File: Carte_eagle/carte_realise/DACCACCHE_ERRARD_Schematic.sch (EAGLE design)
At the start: 10 parts, among them CON1 CON-1X2-SPOX-M-2.50, CON2 CON-1X2-SPOX-M-2.50, U1 DOGM163

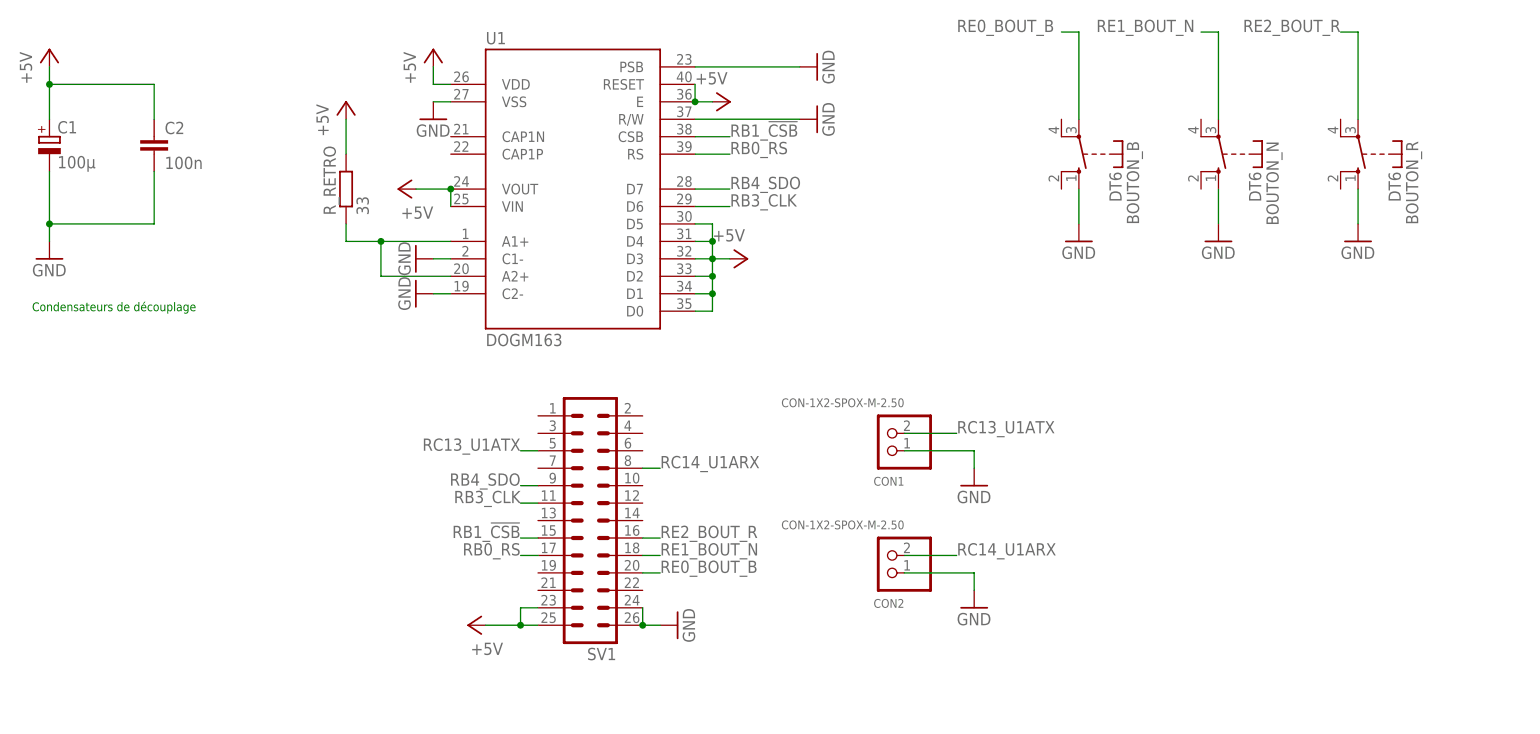
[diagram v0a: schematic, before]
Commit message: Modification de schematics eagle
Rajout des commentaires sur le schéma
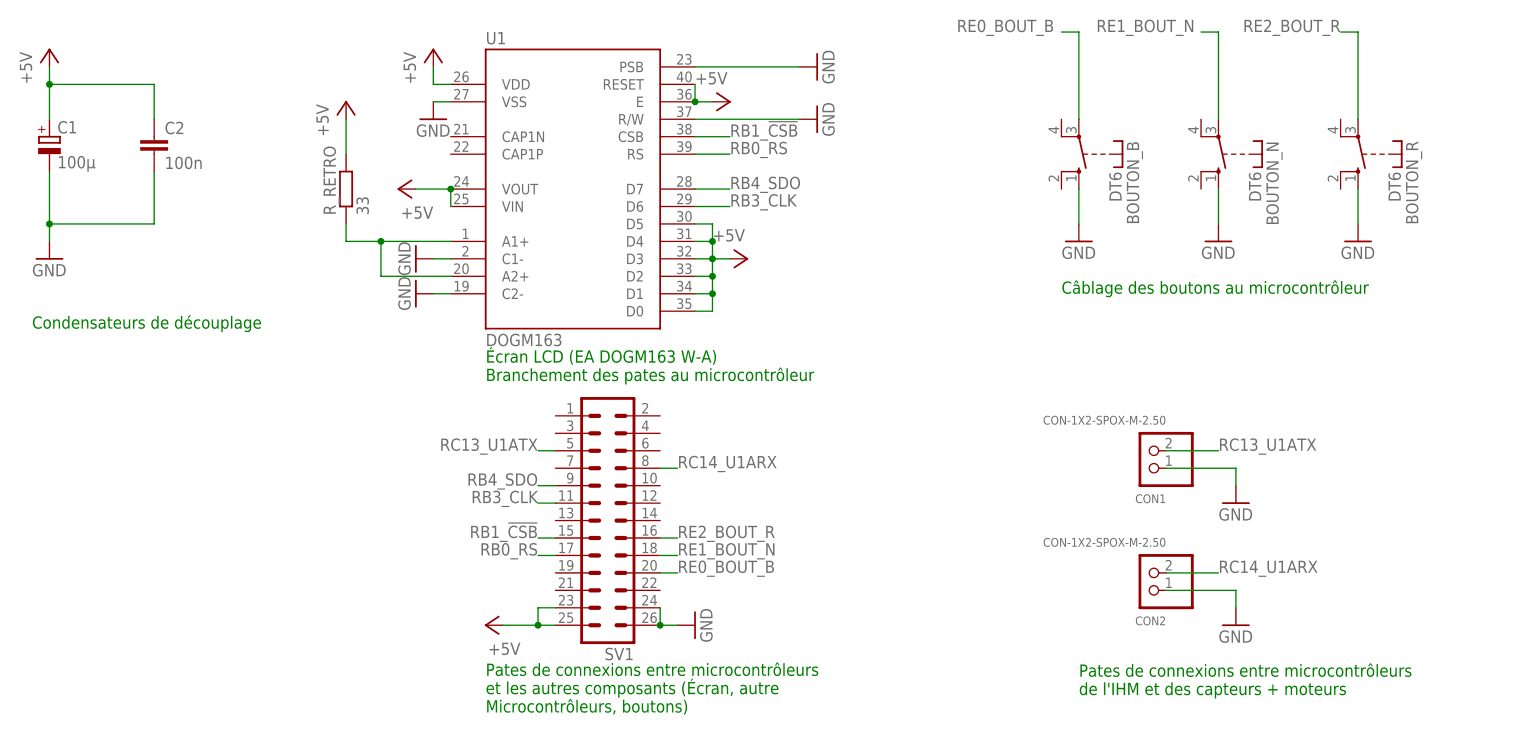
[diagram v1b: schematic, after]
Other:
- note added: "Câblage des boutons au microcontrôleur"
- note added: "Pates de connexions entre microcontrôleurs de l'IHM et des capteurs + moteurs"
- note added: "Pates de connexions entre microcontrôleurs et les autres composants (Écran, autre Microcontrôleurs, boutons)"
- note added: "Écran LCD (EA DOGM163 W-A) Branchement des pates au microcontrôleur"
- moved on the sheet: CON1, CON2, SV1
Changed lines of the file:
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@@
 <sheet>
 <plain>
-<text x="-20.32" y="38.1" size="1.27" layer="91">Condensateurs de découplage</text>
+<text x="45.72" y="27.94" size="1.778" layer="91">Écran LCD (EA DOGM163 W-A)
+Branchement des pates au microcontrôleur</text>
+<text x="129.54" y="40.64" size="1.778" layer="91">Câblage des boutons au microcontrôleur</text>
+<text x="132.08" y="-17.78" size="1.778" layer="91">Pates de connexions entre microcontrôleurs
+de l'IHM et des capteurs + moteurs</text>
+<text x="45.72" y="-20.32" size="1.778" layer="91">Pates de connexions entre microcontrôleurs
+et les autres composants (Écran, autre
+Microcontrôleurs, boutons)</text>
+<text x="-20.32" y="35.56" size="1.778" layer="91">Condensateurs de découplage</text>
 </plain>
 <instances>
 <instance part="U1" gate="G$1" x="58.42" y="55.88"/>
-<instance part="SV1" gate="1" x="60.96" y="7.62" rot="R180"/>
+<instance part="SV1" gate="1" x="63.5" y="7.62" rot="R180"/>
 <instance part="GND2" gate="1" x="93.98" y="73.66" rot="R90"/>
-<instance part="GND3" gate="1" x="73.66" y="-7.62" rot="R90"/>
+<instance part="GND3" gate="1" x="76.2" y="-7.62" rot="R90"/>
 <instance part="P+1" gate="1" x="33.02" y="55.88" rot="R90"/>
 <instance part="P+2" gate="1" x="81.28" y="68.58" rot="R270"/>
@@
 <instance part="GND7" gate="1" x="152.4" y="48.26"/>
 <instance part="GND8" gate="1" x="132.08" y="48.26"/>
-<instance part="GND10" gate="1" x="116.84" y="12.7"/>
-<instance part="CON1" gate="G$1" x="104.14" y="20.32" rot="R180"/>
-<instance part="CON2" gate="G$1" x="104.14" y="2.54" rot="R180"/>
-<instance part="P+9" gate="1" x="43.18" y="-7.62" rot="R90"/>
+<instance part="GND10" gate="1" x="154.94" y="10.16"/>
+<instance part="CON1" gate="G$1" x="142.24" y="17.78" rot="R180"/>
+<instance part="CON2" gate="G$1" x="142.24" y="0" rot="R180"/>
+<instance part="P+9" gate="1" x="45.72" y="-7.62" rot="R90"/>
 <instance part="C2" gate="G$1" x="-2.54" y="63.5"/>
-<instance part="GND9" gate="1" x="116.84" y="-5.08"/>
+<instance part="GND9" gate="1" x="154.94" y="-7.62"/>
 <instance part="GND11" gate="1" x="35.56" y="40.64" rot="R270"/>
 <instance part="GND12" gate="1" x="35.56" y="45.72" rot="R270"/>
@@
 <pinref part="P+9" gate="1" pin="+5V"/>
 <pinref part="SV1" gate="1" pin="25"/>
-<wire x1="45.72" y1="-7.62" x2="50.8" y2="-7.62" width="0.1524" layer="91"/>
+<wire x1="48.26" y1="-7.62" x2="53.34" y2="-7.62" width="0.1524" layer="91"/>
 <pinref part="SV1" gate="1" pin="23"/>
-<wire x1="50.8" y1="-7.62" x2="53.34" y2="-7.62" width="0.1524" layer="91"/>
-<wire x1="53.34" y1="-5.08" x2="50.8" y2="-5.08" width="0.1524" layer="91"/>
-<wire x1="50.8" y1="-5.08" x2="50.8" y2="-7.62" width="0.1524" layer="91"/>
-<junction x="50.8" y="-7.62"/>
+<wire x1="53.34" y1="-7.62" x2="55.88" y2="-7.62" width="0.1524" layer="91"/>
+<wire x1="55.88" y1="-5.08" x2="53.34" y2="-5.08" width="0.1524" layer="91"/>
+<wire x1="53.34" y1="-5.08" x2="53.34" y2="-7.62" width="0.1524" layer="91"/>
+<junction x="53.34" y="-7.62"/>
 </segment>
 <segment>
@@
 <pinref part="SV1" gate="1" pin="24"/>
 <pinref part="SV1" gate="1" pin="26"/>
-<wire x1="68.58" y1="-5.08" x2="68.58" y2="-7.62" width="0.1524" layer="91"/>
+<wire x1="71.12" y1="-5.08" x2="71.12" y2="-7.62" width="0.1524" layer="91"/>
 <pinref part="GND3" gate="1" pin="GND"/>
-<wire x1="71.12" y1="-7.62" x2="68.58" y2="-7.62" width="0.1524" layer="91"/>
-<junction x="68.58" y="-7.62"/>
+<wire x1="73.66" y1="-7.62" x2="71.12" y2="-7.62" width="0.1524" layer="91"/>
+<junction x="71.12" y="-7.62"/>
 </segment>
 <segment>
@@
 <segment>
 <pinref part="GND9" gate="1" pin="GND"/>
-<wire x1="116.84" y1="0" x2="116.84" y2="-2.54" width="0.1524" layer="91"/>
+<wire x1="154.94" y1="-2.54" x2="154.94" y2="-5.08" width="0.1524" layer="91"/>
 <pinref part="CON2" gate="G$1" pin="1"/>
-<wire x1="106.68" y1="0" x2="116.84" y2="0" width="0.1524" layer="91"/>
+<wire x1="144.78" y1="-2.54" x2="154.94" y2="-2.54" width="0.1524" layer="91"/>
 </segment>
 <segment>
 <pinref part="GND10" gate="1" pin="GND"/>
 <pinref part="CON1" gate="G$1" pin="1"/>
-<wire x1="106.68" y1="17.78" x2="116.84" y2="17.78" width="0.1524" layer="91"/>
-<wire x1="116.84" y1="17.78" x2="116.84" y2="15.24" width="0.1524" layer="91"/>
+<wire x1="144.78" y1="15.24" x2="154.94" y2="15.24" width="0.1524" layer="91"/>
+<wire x1="154.94" y1="15.24" x2="154.94" y2="12.7" width="0.1524" layer="91"/>
 </segment>
 <segment>
@@
 <segment>
 <pinref part="SV1" gate="1" pin="9"/>
-<wire x1="53.34" y1="12.7" x2="50.8" y2="12.7" width="0.1524" layer="91"/>
-<label x="50.8" y="12.7" size="1.778" layer="95" rot="MR0"/>
+<wire x1="55.88" y1="12.7" x2="53.34" y2="12.7" width="0.1524" layer="91"/>
+<label x="53.34" y="12.7" size="1.778" layer="95" rot="MR0"/>
 </segment>
 <segment>
@@
 <segment>
 <pinref part="SV1" gate="1" pin="11"/>
-<wire x1="53.34" y1="10.16" x2="50.8" y2="10.16" width="0.1524" layer="91"/>
-<label x="50.8" y="10.16" size="1.778" layer="95" rot="MR0"/>
+<wire x1="55.88" y1="10.16" x2="53.34" y2="10.16" width="0.1524" layer="91"/>
+<label x="53.34" y="10.16" size="1.778" layer="95" rot="MR0"/>
 </segment>
 <segment>
@@
 <segment>
 <pinref part="SV1" gate="1" pin="15"/>
-<wire x1="53.34" y1="5.08" x2="50.8" y2="5.08" width="0.1524" layer="91"/>
-<label x="50.8" y="5.08" size="1.778" layer="95" rot="MR0"/>
+<wire x1="55.88" y1="5.08" x2="53.34" y2="5.08" width="0.1524" layer="91"/>
+<label x="53.34" y="5.08" size="1.778" layer="95" rot="MR0"/>
 </segment>
 <segment>
@@
 <segment>
 <pinref part="SV1" gate="1" pin="17"/>
-<wire x1="53.34" y1="2.54" x2="50.8" y2="2.54" width="0.1524" layer="91"/>
-<label x="50.8" y="2.54" size="1.778" layer="95" rot="MR0"/>
+<wire x1="55.88" y1="2.54" x2="53.34" y2="2.54" width="0.1524" layer="91"/>
+<label x="53.34" y="2.54" size="1.778" layer="95" rot="MR0"/>
 </segment>
 <segment>
@@
 <segment>
 <pinref part="SV1" gate="1" pin="16"/>
-<wire x1="68.58" y1="5.08" x2="71.12" y2="5.08" width="0.1524" layer="91"/>
-<label x="71.12" y="5.08" size="1.778" layer="95"/>
+<wire x1="71.12" y1="5.08" x2="73.66" y2="5.08" width="0.1524" layer="91"/>
+<label x="73.66" y="5.08" size="1.778" layer="95"/>
 </segment>
 <segment>
@@
 <segment>
 <pinref part="SV1" gate="1" pin="18"/>
-<wire x1="68.58" y1="2.54" x2="71.12" y2="2.54" width="0.1524" layer="91"/>
-<label x="71.12" y="2.54" size="1.778" layer="95"/>
+<wire x1="71.12" y1="2.54" x2="73.66" y2="2.54" width="0.1524" layer="91"/>
+<label x="73.66" y="2.54" size="1.778" layer="95"/>
 </segment>
 <segment>
@@
 <segment>
 <pinref part="SV1" gate="1" pin="20"/>
-<wire x1="68.58" y1="0" x2="71.12" y2="0" width="0.1524" layer="91"/>
-<label x="71.12" y="0" size="1.778" layer="95"/>
+<wire x1="71.12" y1="0" x2="73.66" y2="0" width="0.1524" layer="91"/>
+<label x="73.66" y="0" size="1.778" layer="95"/>
 </segment>
 <segment>
@@
 <segment>
 <pinref part="SV1" gate="1" pin="5"/>
-<wire x1="53.34" y1="17.78" x2="50.8" y2="17.78" width="0.1524" layer="91"/>
-<label x="50.8" y="17.78" size="1.778" layer="95" rot="MR0"/>
+<wire x1="55.88" y1="17.78" x2="53.34" y2="17.78" width="0.1524" layer="91"/>
+<label x="53.34" y="17.78" size="1.778" layer="95" rot="MR0"/>
 </segment>
 <segment>
 <pinref part="CON1" gate="G$1" pin="2"/>
-<wire x1="106.68" y1="20.32" x2="114.3" y2="20.32" width="0.1524" layer="91"/>
-<label x="114.3" y="20.32" size="1.778" layer="95"/>
+<wire x1="144.78" y1="17.78" x2="152.4" y2="17.78" width="0.1524" layer="91"/>
+<label x="152.4" y="17.78" size="1.778" layer="95"/>
 </segment>
 </net>
@@
 <segment>
 <pinref part="SV1" gate="1" pin="8"/>
-<wire x1="68.58" y1="15.24" x2="71.12" y2="15.24" width="0.1524" layer="91"/>
-<label x="71.12" y="15.24" size="1.778" layer="95"/>
+<wire x1="71.12" y1="15.24" x2="73.66" y2="15.24" width="0.1524" layer="91"/>
+<label x="73.66" y="15.24" size="1.778" layer="95"/>
 </segment>
 <segment>
 <pinref part="CON2" gate="G$1" pin="2"/>
-<wire x1="106.68" y1="2.54" x2="114.3" y2="2.54" width="0.1524" layer="91"/>
-<label x="114.3" y="2.54" size="1.778" layer="95"/>
+<wire x1="144.78" y1="0" x2="152.4" y2="0" width="0.1524" layer="91"/>
+<label x="152.4" y="0" size="1.778" layer="95"/>
 </segment>
 </net>
@@
 </schematic>
 </drawing>
+<compatibility>
+<note version="6.3" minversion="6.2.2" severity="warning">
+Since Version 6.2.2 text objects can contain more than one line,
+which will not be processed correctly with this version.
+</note>
+</compatibility>
 </eagle>

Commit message: update board et schematics
finalisation du schema avec le changement des pins de l'ecran et des boutons
finalisation de la carte avec l'epaisseur des cables et le cassage des angles droits
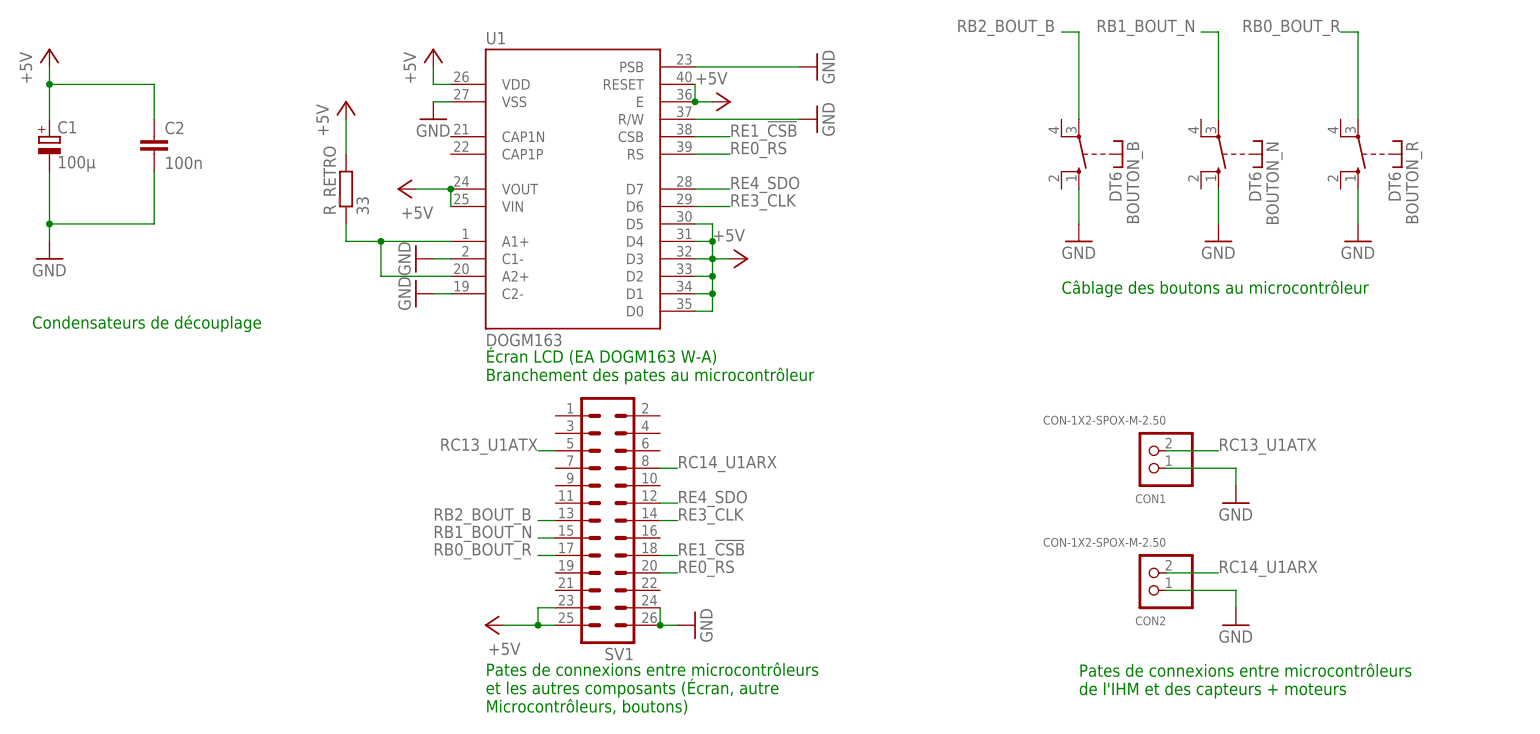
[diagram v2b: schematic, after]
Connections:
- net N$1 renamed RHETRO_RES
- removed net RB0_RS: SV1.17, U1.RS
- removed net RB1_!CSB: SV1.15, U1.CSB
- removed net RB3_CLK: SV1.11, U1.D6
- removed net RB4_SDO: SV1.9, U1.D7
- removed net RE0_BOUT_B: BOUTON_B.P, SV1.20
- removed net RE1_BOUT_N: BOUTON_N.P, SV1.18
- removed net RE2_BOUT_R: BOUTON_R.P, SV1.16
- new net RB0_BOUT_R: BOUTON_R.P, SV1.17
- new net RB1_BOUT_N: BOUTON_N.P, SV1.15
- new net RB2_BOUT_B: BOUTON_B.P, SV1.13
- new net RE0_RS: SV1.20, U1.RS
- new net RE1_!CSB: SV1.18, U1.CSB
- new net RE3_CLK: SV1.14, U1.D6
- new net RE4_SDO: SV1.12, U1.D7
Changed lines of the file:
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@@
 </segment>
 </net>
-<net name="RB4_SDO" class="0">
-<segment>
-<pinref part="SV1" gate="1" pin="9"/>
-<wire x1="55.88" y1="12.7" x2="53.34" y2="12.7" width="0.1524" layer="91"/>
-<label x="53.34" y="12.7" size="1.778" layer="95" rot="MR0"/>
-</segment>
-<segment>
-<pinref part="U1" gate="G$1" pin="D7"/>
-<wire x1="76.2" y1="55.88" x2="81.28" y2="55.88" width="0.1524" layer="91"/>
-<label x="81.28" y="55.88" size="1.778" layer="95"/>
-</segment>
-</net>
-<net name="RB3_CLK" class="0">
-<segment>
-<pinref part="SV1" gate="1" pin="11"/>
-<wire x1="55.88" y1="10.16" x2="53.34" y2="10.16" width="0.1524" layer="91"/>
-<label x="53.34" y="10.16" size="1.778" layer="95" rot="MR0"/>
-</segment>
-<segment>
-<pinref part="U1" gate="G$1" pin="D6"/>
-<wire x1="76.2" y1="53.34" x2="81.28" y2="53.34" width="0.1524" layer="91"/>
-<label x="81.28" y="53.34" size="1.778" layer="95"/>
-</segment>
-</net>
-<net name="RB1_!CSB" class="0">
-<segment>
-<pinref part="SV1" gate="1" pin="15"/>
-<wire x1="55.88" y1="5.08" x2="53.34" y2="5.08" width="0.1524" layer="91"/>
-<label x="53.34" y="5.08" size="1.778" layer="95" rot="MR0"/>
-</segment>
-<segment>
-<pinref part="U1" gate="G$1" pin="CSB"/>
-<wire x1="76.2" y1="63.5" x2="81.28" y2="63.5" width="0.1524" layer="91"/>
-<label x="81.28" y="63.5" size="1.778" layer="95"/>
-</segment>
-</net>
-<net name="RB0_RS" class="0">
-<segment>
-<pinref part="SV1" gate="1" pin="17"/>
-<wire x1="55.88" y1="2.54" x2="53.34" y2="2.54" width="0.1524" layer="91"/>
-<label x="53.34" y="2.54" size="1.778" layer="95" rot="MR0"/>
-</segment>
-<segment>
-<pinref part="U1" gate="G$1" pin="RS"/>
-<wire x1="76.2" y1="60.96" x2="81.28" y2="60.96" width="0.1524" layer="91"/>
-<label x="81.28" y="60.96" size="1.778" layer="95"/>
-</segment>
-</net>
-<net name="RE2_BOUT_R" class="0">
-<segment>
-<pinref part="SV1" gate="1" pin="16"/>
-<wire x1="71.12" y1="5.08" x2="73.66" y2="5.08" width="0.1524" layer="91"/>
-<label x="73.66" y="5.08" size="1.778" layer="95"/>
-</segment>
+<net name="RB0_BOUT_R" class="0">
 <segment>
 <wire x1="170.18" y1="78.74" x2="172.72" y2="78.74" width="0.1524" layer="91"/>
@@
 <pinref part="BOUTON_R" gate="1" pin="P"/>
 </segment>
+<segment>
+<pinref part="SV1" gate="1" pin="17"/>
+<wire x1="55.88" y1="2.54" x2="53.34" y2="2.54" width="0.1524" layer="91"/>
+<label x="38.1" y="2.54" size="1.778" layer="95"/>
+</segment>
 </net>
-<net name="RE1_BOUT_N" class="0">
-<segment>
-<pinref part="SV1" gate="1" pin="18"/>
-<wire x1="71.12" y1="2.54" x2="73.66" y2="2.54" width="0.1524" layer="91"/>
-<label x="73.66" y="2.54" size="1.778" layer="95"/>
-</segment>
+<net name="RB1_BOUT_N" class="0">
 <segment>
 <pinref part="BOUTON_N" gate="1" pin="P"/>
@@
 <label x="134.62" y="78.74" size="1.778" layer="95"/>
 </segment>
+<segment>
+<pinref part="SV1" gate="1" pin="15"/>
+<wire x1="55.88" y1="5.08" x2="53.34" y2="5.08" width="0.1524" layer="91"/>
+<label x="38.1" y="5.08" size="1.778" layer="95"/>
+</segment>
 </net>
-<net name="RE0_BOUT_B" class="0">
-<segment>
-<pinref part="SV1" gate="1" pin="20"/>
-<wire x1="71.12" y1="0" x2="73.66" y2="0" width="0.1524" layer="91"/>
-<label x="73.66" y="0" size="1.778" layer="95"/>
-</segment>
+<net name="RB2_BOUT_B" class="0">
 <segment>
 <pinref part="BOUTON_B" gate="1" pin="P"/>
@@
 <label x="114.3" y="78.74" size="1.778" layer="95"/>
 </segment>
+<segment>
+<pinref part="SV1" gate="1" pin="13"/>
+<wire x1="55.88" y1="7.62" x2="53.34" y2="7.62" width="0.1524" layer="91"/>
+<label x="38.1" y="7.62" size="1.778" layer="95"/>
+</segment>
 </net>
-<net name="N$1" class="0">
+<net name="RHETRO_RES" class="0">
 <segment>
 <pinref part="R_RETRO" gate="G$1" pin="1"/>
@@
 </segment>
 </net>
+<net name="RE1_!CSB" class="0">
+<segment>
+<pinref part="U1" gate="G$1" pin="CSB"/>
+<wire x1="76.2" y1="63.5" x2="81.28" y2="63.5" width="0.1524" layer="91"/>
+<label x="81.28" y="63.5" size="1.778" layer="95"/>
+</segment>
+<segment>
+<pinref part="SV1" gate="1" pin="18"/>
+<wire x1="71.12" y1="2.54" x2="73.66" y2="2.54" width="0.1524" layer="91"/>
+<label x="73.66" y="2.54" size="1.778" layer="95"/>
+</segment>
+</net>
+<net name="RE0_RS" class="0">
+<segment>
+<pinref part="U1" gate="G$1" pin="RS"/>
+<wire x1="76.2" y1="60.96" x2="81.28" y2="60.96" width="0.1524" layer="91"/>
+<label x="81.28" y="60.96" size="1.778" layer="95"/>
+</segment>
+<segment>
+<pinref part="SV1" gate="1" pin="20"/>
+<wire x1="71.12" y1="0" x2="73.66" y2="0" width="0.1524" layer="91"/>
+<label x="73.66" y="0" size="1.778" layer="95"/>
+</segment>
+</net>
+<net name="RE4_SDO" class="0">
+<segment>
+<pinref part="U1" gate="G$1" pin="D7"/>
+<wire x1="76.2" y1="55.88" x2="81.28" y2="55.88" width="0.1524" layer="91"/>
+<label x="81.28" y="55.88" size="1.778" layer="95"/>
+</segment>
+<segment>
+<pinref part="SV1" gate="1" pin="12"/>
+<wire x1="71.12" y1="10.16" x2="73.66" y2="10.16" width="0.1524" layer="91"/>
+<label x="73.66" y="10.16" size="1.778" layer="95"/>
+</segment>
+</net>
+<net name="RE3_CLK" class="0">
+<segment>
+<pinref part="U1" gate="G$1" pin="D6"/>
+<wire x1="76.2" y1="53.34" x2="81.28" y2="53.34" width="0.1524" layer="91"/>
+<label x="81.28" y="53.34" size="1.778" layer="95"/>
+</segment>
+<segment>
+<pinref part="SV1" gate="1" pin="14"/>
+<wire x1="71.12" y1="7.62" x2="73.66" y2="7.62" width="0.1524" layer="91"/>
+<label x="73.66" y="7.62" size="1.778" layer="95"/>
+</segment>
+</net>
